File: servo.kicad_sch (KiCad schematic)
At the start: 27 parts, among them J17 Conn_04x03_Servo, J18 Conn_04x03_Servo, J19 Conn_04x03_Servo, J20 Conn_04x03_Servo, U3 PCA9685PW

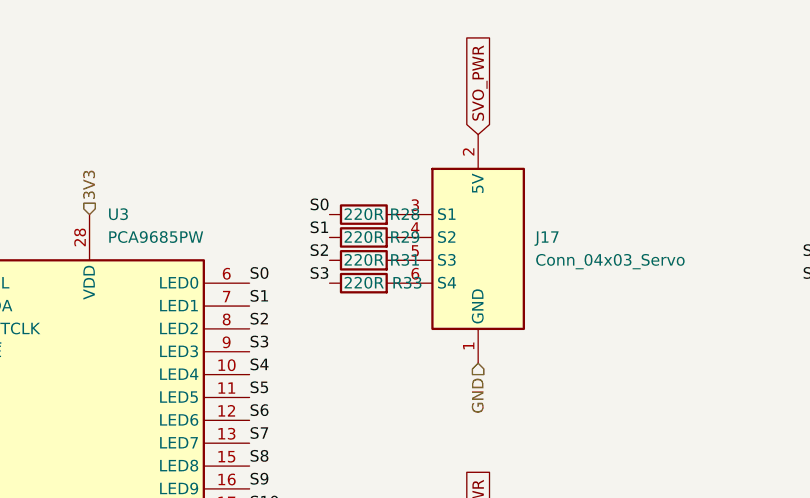
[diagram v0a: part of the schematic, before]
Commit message: Fix incorrect resistor value
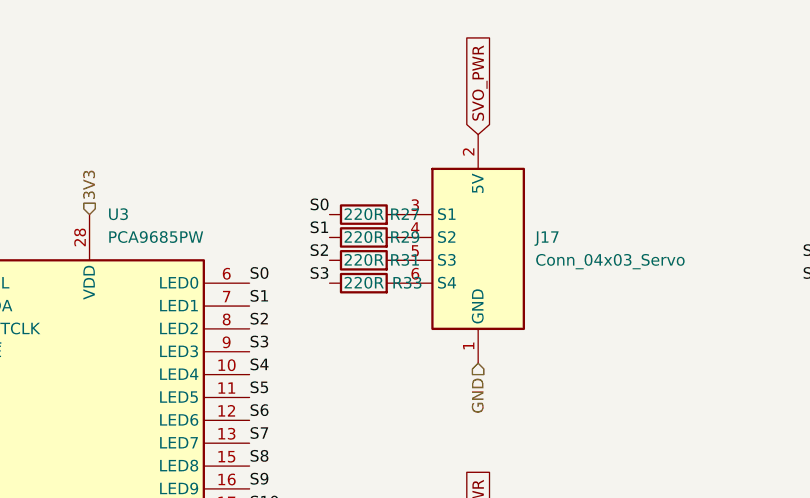
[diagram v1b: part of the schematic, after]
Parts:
- renumbered R28 to R27
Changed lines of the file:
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@@
 		(on_board yes)
 		(dnp no)
-		(property "Reference" "R28"
+		(property "Reference" "R27"
 			(at 155.702 73.66 90)
 			(effects
